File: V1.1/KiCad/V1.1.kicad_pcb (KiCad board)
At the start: 2 copper layers, 76.2 x 80.2 mm, 43 parts, among them SW1 SW_Push, U1 ATmega32U4-AU, U2 SRV05-4, Y1 16MHz

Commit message: Added images, organized files
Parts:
- moved R3 5.59 mm to (135.1, 87.3)
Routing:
- net Net-(R3-Pad2): track 24.9 -> 21.8 mm
- net VCC: track 17.7 -> 16.3 mm, vias 3 -> 2
- net GND: track 92.8 -> 94.0 mm
- net +5V: track 103.4 -> 102.2 mm

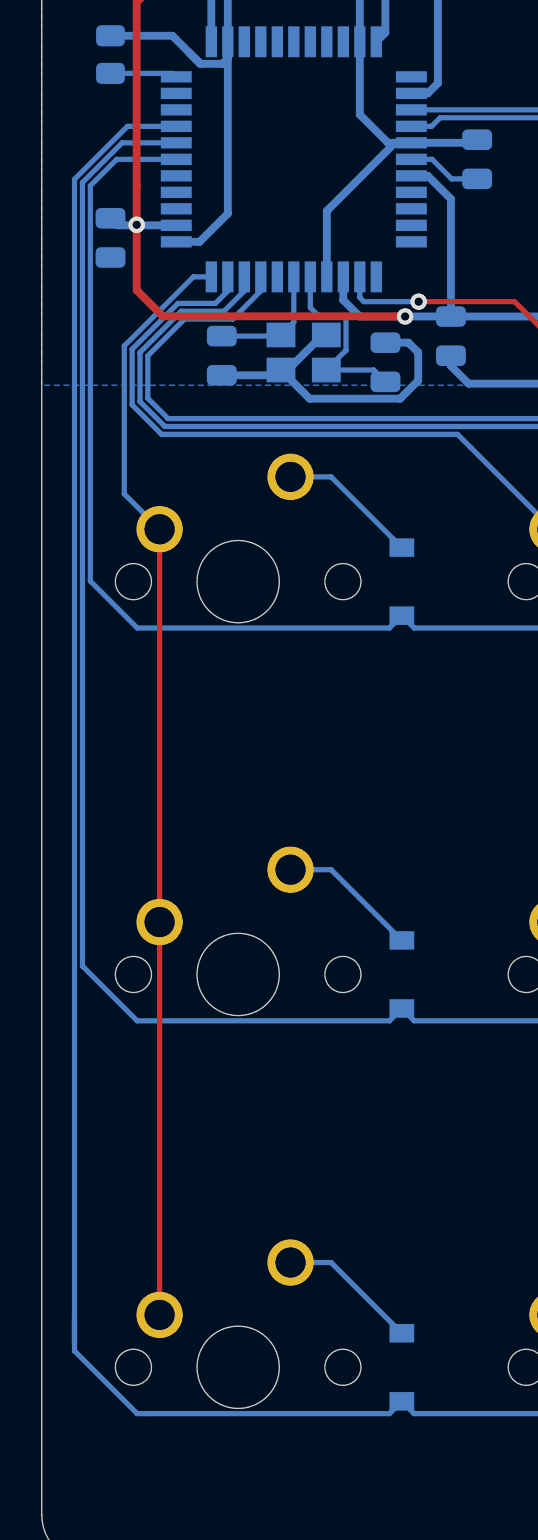
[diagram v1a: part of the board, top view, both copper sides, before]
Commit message: Updated traces to not be as close to decoupling capacitor
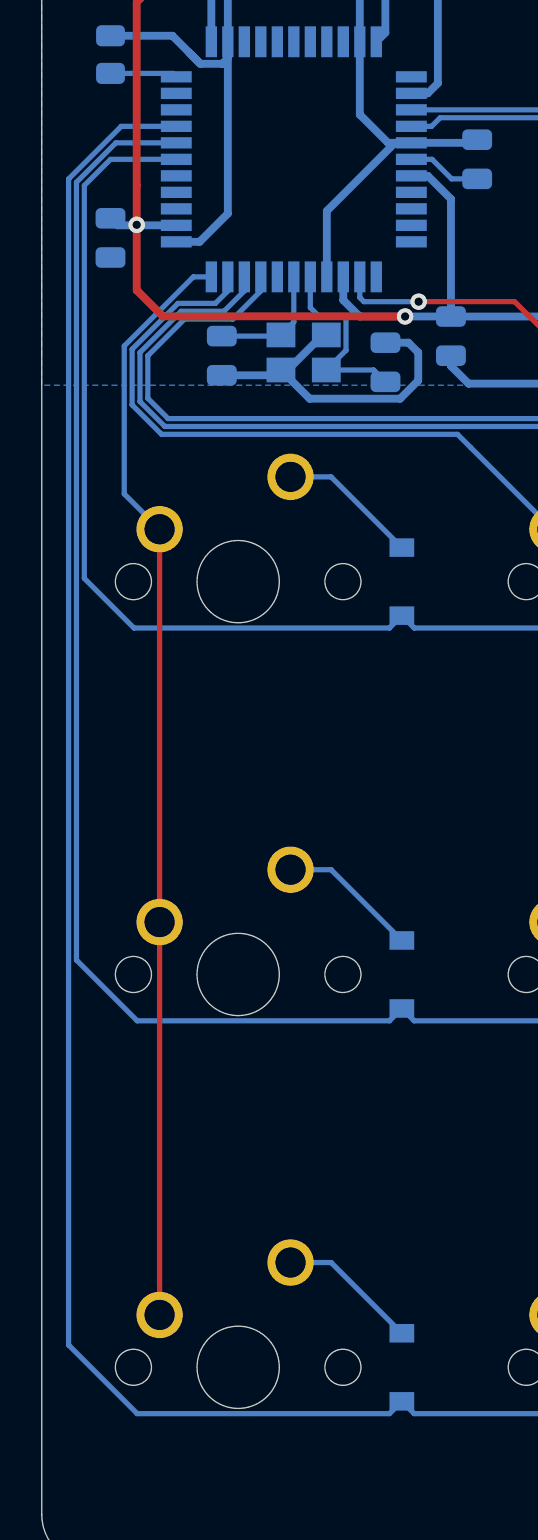
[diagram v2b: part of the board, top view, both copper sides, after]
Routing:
- net ROW2: track 140.0 -> 139.2 mm
- net ROW0: track 99.1 -> 99.6 mm
